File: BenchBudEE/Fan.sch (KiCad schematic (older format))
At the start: 9 parts

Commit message: Revisiting the current/fan module.
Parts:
- removed R? (x3): R, ~, symbol R
- removed RV?: POT, ~, symbol POT
- added D?: DIODE, ~, symbol DIODE
- added Q? (x2): MOSFET_N, ~, symbol MOSFET_N
- added TH?: THERMISTOR, ~, symbol THERMISTOR
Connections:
- net labels added: +12C, FAN_MODE, FAN_PWM
- net labels removed: FAN_EN_N
- wire segments 31 -> 32
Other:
- note added: "+12C non-filtered / non-current-limited"
- note added: "Filtered Rail (12V)"
- note added: "Load/Field"
- note added: "Mosfet is used to select\nVoltage or Current mode here"
- note added: "This PTC will limit max current\nthrough load."
- moved on the sheet: R?
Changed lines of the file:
@@
 $Descr A4 11693 8268
 encoding utf-8
-Sheet 9 9
+Sheet 7 9
 Title ""
-Date "10 feb 2014"
+Date "12 feb 2014"
 Rev ""
 Comp ""
@@
 Comment4 ""
 $EndDescr
-Text HLabel 10650 3700 0    60   Output ~ 0
+Text HLabel 10500 1450 2    60   Output ~ 0
 FAN_OUT+
-Text HLabel 10650 4050 0    60   Output ~ 0
+Text HLabel 10500 1750 2    60   Output ~ 0
 FAN_OUT-
-Text HLabel 10650 4500 0    60   Input ~ 0
+Text HLabel 10500 6000 2    60   Input ~ 0
 TACH_IN
-Text HLabel 1400 5600 0    60   Output ~ 0
+Text HLabel 1400 6000 0    60   Output ~ 0
 TACH_MEAS
 Text HLabel 1400 3950 0    60   Input ~ 0
-FAN_EN_N
+FAN_PWM
 $Comp
 L LM324 U?
@@
 	1    0    0    -1
 $EndComp
-$Comp
-L +12V #PWR?
-U 1 1 52F362D2
-P 7800 1700
-F 0 "#PWR?" H 7800 1650 20  0001 C CNN
-F 1 "+12V" H 7800 1800 30  0000 C CNN
-F 2 "" H 7800 1700 60  0000 C CNN
-F 3 "" H 7800 1700 60  0000 C CNN
-	1    7800 1700
-	1    0    0    -1
-$EndComp
 Wire Wire Line
 	6850 2700 7500 2700
 Wire Wire Line
-	7800 2900 7800 3700
-Wire Wire Line
-	7800 3700 10650 3700
-Wire Wire Line
-	5500 4050 10650 4050
-Wire Wire Line
-	7800 4050 7800 4300
+	7800 2900 7800 4400
 $Comp
 L R R?
 U 1 1 52F362F4
-P 7800 4550
-F 0 "R?" V 7880 4550 40  0000 C CNN
-F 1 "R" V 7807 4551 40  0000 C CNN
-F 2 "~" V 7730 4550 30  0000 C CNN
-F 3 "~" H 7800 4550 30  0000 C CNN
-	1    7800 4550
+P 7800 4650
+F 0 "R?" V 7880 4650 40  0000 C CNN
+F 1 "R" V 7807 4651 40  0000 C CNN
+F 2 "~" V 7730 4650 30  0000 C CNN
+F 3 "~" H 7800 4650 30  0000 C CNN
+	1    7800 4650
 	1    0    0    -1
 $EndComp
@@
 $EndComp
 Wire Wire Line
-	7800 5300 7800 4800
+	7800 5300 7800 4900
 Wire Wire Line
 	5500 4050 5500 2800
@@
 	5500 2800 5850 2800
 Connection ~ 7800 4050
-Wire Wire Line
-	7800 2500 7800 1700
 $Comp
 L +12V #PWR?
@@
 	4400 2600 5850 2600
 $Comp
-L R R?
-U 1 1 52F3640C
-P 4700 2200
-F 0 "R?" V 4780 2200 40  0000 C CNN
-F 1 "R" V 4707 2201 40  0000 C CNN
-F 2 "~" V 4630 2200 30  0000 C CNN
-F 3 "~" H 4700 2200 30  0000 C CNN
-	1    4700 2200
-	1    0    0    -1
-$EndComp
-$Comp
-L +12V #PWR?
-U 1 1 52F36412
-P 4700 1750
-F 0 "#PWR?" H 4700 1700 20  0001 C CNN
-F 1 "+12V" H 4700 1850 30  0000 C CNN
-F 2 "" H 4700 1750 60  0000 C CNN
-F 3 "" H 4700 1750 60  0000 C CNN
-	1    4700 1750
-	1    0    0    -1
-$EndComp
-Wire Wire Line
-	4700 1750 4700 1950
-Wire Wire Line
-	4700 2450 4700 2900
-$Comp
-L POT RV?
-U 1 1 52F36438
-P 4700 3150
-F 0 "RV?" H 4700 3050 50  0000 C CNN
-F 1 "POT" H 4700 3150 50  0000 C CNN
-F 2 "~" H 4700 3150 60  0000 C CNN
-F 3 "~" H 4700 3150 60  0000 C CNN
-	1    4700 3150
-	0    -1   -1   0
-$EndComp
-Connection ~ 4700 2600
-$Comp
 L AGND #PWR?
 U 1 1 52F36460
-P 4700 3700
-F 0 "#PWR?" H 4700 3700 40  0001 C CNN
-F 1 "AGND" H 4700 3630 50  0000 C CNN
-F 2 "" H 4700 3700 60  0000 C CNN
-F 3 "" H 4700 3700 60  0000 C CNN
-	1    4700 3700
-	1    0    0    -1
-$EndComp
-Wire Wire Line
-	4700 3700 4700 3400
+P 5150 3700
+F 0 "#PWR?" H 5150 3700 40  0001 C CNN
+F 1 "AGND" H 5150 3630 50  0000 C CNN
+F 2 "" H 5150 3700 60  0000 C CNN
+F 3 "" H 5150 3700 60  0000 C CNN
+	1    5150 3700
+	1    0    0    -1
+$EndComp
 $Comp
 L MCP4922-E/P U?
@@
 	1    0    0    -1
 $EndComp
-Wire Wire Line
-	10650 4500 9500 4500
-Wire Wire Line
-	9500 4500 9500 5850
-Wire Wire Line
-	9500 5850 2050 5850
 Text HLabel 1400 4200 0    60   Output ~ 0
 CURR_MEAS
 Wire Wire Line
-	2050 5850 2050 5600
-Wire Wire Line
 	1400 4200 7800 4200
 Connection ~ 7800 4200
-Wire Wire Line
-	2050 5600 1400 5600
 Connection ~ 5150 2600
 Wire Wire Line
-	1400 3950 5150 3950
-$Comp
-L R R?
-U 1 1 52F36597
-P 5150 3150
-F 0 "R?" V 5230 3150 40  0000 C CNN
-F 1 "R" V 5157 3151 40  0000 C CNN
-F 2 "~" V 5080 3150 30  0000 C CNN
-F 3 "~" H 5150 3150 30  0000 C CNN
-	1    5150 3150
-	1    0    0    -1
-$EndComp
-Wire Wire Line
-	5150 2900 5150 2600
-Wire Wire Line
-	5150 3950 5150 3400
+	5150 2600 5150 2950
 $Comp
 L R R?
@@
 Wire Wire Line
 	1400 2750 2400 2750
-$Comp
-L R R?
-U 1 1 52F36679
-P 2200 3400
-F 0 "R?" V 2280 3400 40  0000 C CNN
-F 1 "R" V 2207 3401 40  0000 C CNN
-F 2 "~" V 2130 3400 30  0000 C CNN
-F 3 "~" H 2200 3400 30  0000 C CNN
-	1    2200 3400
-	1    0    0    -1
-$EndComp
-Wire Wire Line
-	2400 2950 2200 2950
-Wire Wire Line
-	2200 2950 2200 3150
-Wire Wire Line
-	2200 3650 2200 3950
-Connection ~ 2200 3950
 Text Notes 2850 1950 0    60   ~ 0
 DAC
+$Comp
+L MOSFET_N Q?
+U 1 1 52FADC41
+P 7200 4650
+F 0 "Q?" H 7210 4820 60  0000 R CNN
+F 1 "MOSFET_N" H 7210 4500 60  0000 R CNN
+F 2 "~" H 7200 4650 60  0000 C CNN
+F 3 "~" H 7200 4650 60  0000 C CNN
+	1    7200 4650
+	1    0    0    -1
+$EndComp
+$Comp
+L THERMISTOR TH?
+U 1 1 52FADC53
+P 7800 1100
+F 0 "TH?" V 7900 1150 50  0000 C CNN
+F 1 "THERMISTOR" V 7700 1100 50  0000 C CNN
+F 2 "~" H 7800 1100 60  0000 C CNN
+F 3 "~" H 7800 1100 60  0000 C CNN
+	1    7800 1100
+	1    0    0    -1
+$EndComp
+Wire Wire Line
+	7800 850  7800 750
+Wire Wire Line
+	7800 1350 7800 1450
+Wire Wire Line
+	7350 1450 10500 1450
+Wire Wire Line
+	10500 1750 7800 1750
+Wire Wire Line
+	7800 1750 7800 2500
+$Comp
+L DIODE D?
+U 1 1 52FADCC6
+P 7350 1650
+F 0 "D?" H 7350 1750 40  0000 C CNN
+F 1 "DIODE" H 7350 1550 40  0000 C CNN
+F 2 "~" H 7350 1650 60  0000 C CNN
+F 3 "~" H 7350 1650 60  0000 C CNN
+	1    7350 1650
+	0    -1   -1   0
+$EndComp
+Wire Wire Line
+	7350 1850 7800 1850
+Connection ~ 7800 1850
+Connection ~ 7800 1450
+Wire Wire Line
+	5500 4050 7800 4050
+Wire Wire Line
+	7800 4050 7800 4100
+Wire Wire Line
+	7300 4450 7300 4350
+Wire Wire Line
+	7300 4350 7800 4350
+Connection ~ 7800 4350
+Wire Wire Line
+	7300 4850 7300 5050
+Wire Wire Line
+	7300 5050 7800 5050
+Connection ~ 7800 5050
+Wire Wire Line
+	1400 6000 10500 6000
+$Comp
+L MOSFET_N Q?
+U 1 1 52FAE0E1
+P 5050 3150
+F 0 "Q?" H 5060 3320 60  0000 R CNN
+F 1 "MOSFET_N" H 5060 3000 60  0000 R CNN
+F 2 "~" H 5050 3150 60  0000 C CNN
+F 3 "~" H 5050 3150 60  0000 C CNN
+	1    5050 3150
+	1    0    0    -1
+$EndComp
+Wire Wire Line
+	5150 3700 5150 3350
+Wire Wire Line
+	1400 3950 4050 3950
+Wire Wire Line
+	4050 3950 4050 3150
+Wire Wire Line
+	4050 3150 4850 3150
+Wire Wire Line
+	7000 4650 1400 4650
+Text HLabel 1400 4650 0    60   Input ~ 0
+FAN_MODE
+Text Notes 5850 1600 0    60   ~ 0
+Filtered Rail (12V)
+$Comp
+L +12C #PWR?
+U 1 1 52FAE969
+P 7800 750
+F 0 "#PWR?" H 7800 720 30  0001 C CNN
+F 1 "+12C" H 7800 860 40  0000 C CNN
+F 2 "" H 7800 750 60  0000 C CNN
+F 3 "" H 7800 750 60  0000 C CNN
+	1    7800 750
+	1    0    0    -1
+$EndComp
+Text Notes 8000 1000 0    60   ~ 0
+This PTC will limit max current\nthrough load.
+Text Notes 10150 1650 0    60   ~ 0
+Load/Field
+Text Notes 8050 4650 0    60   ~ 0
+Mosfet is used to select\nVoltage or Current mode here
+Text Notes 7950 650  0    60   ~ 0
++12C non-filtered / non-current-limited
 $EndSCHEMATC

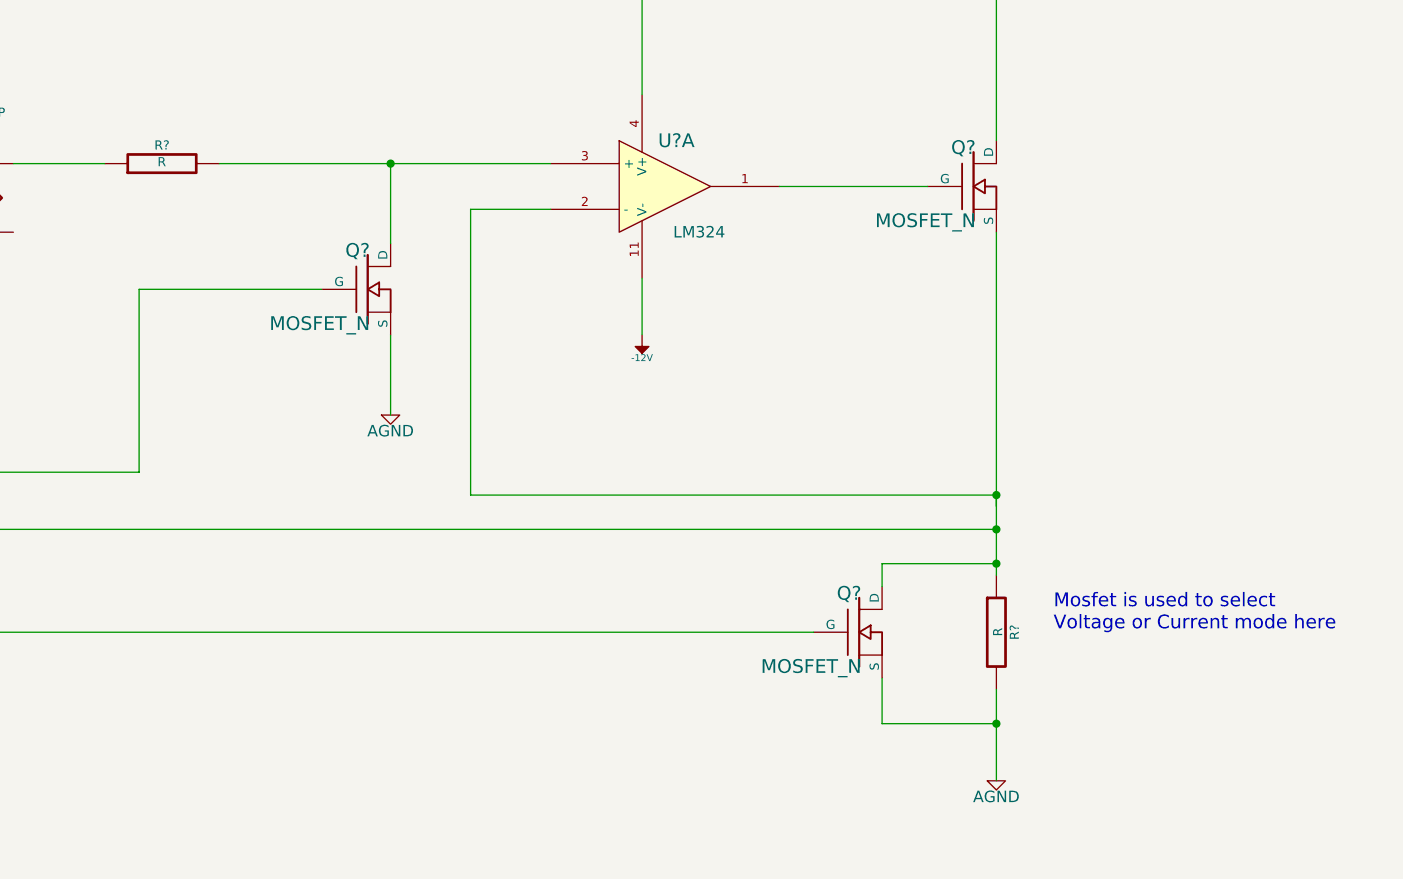
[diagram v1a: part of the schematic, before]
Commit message: Documented the fan driver mosfets.
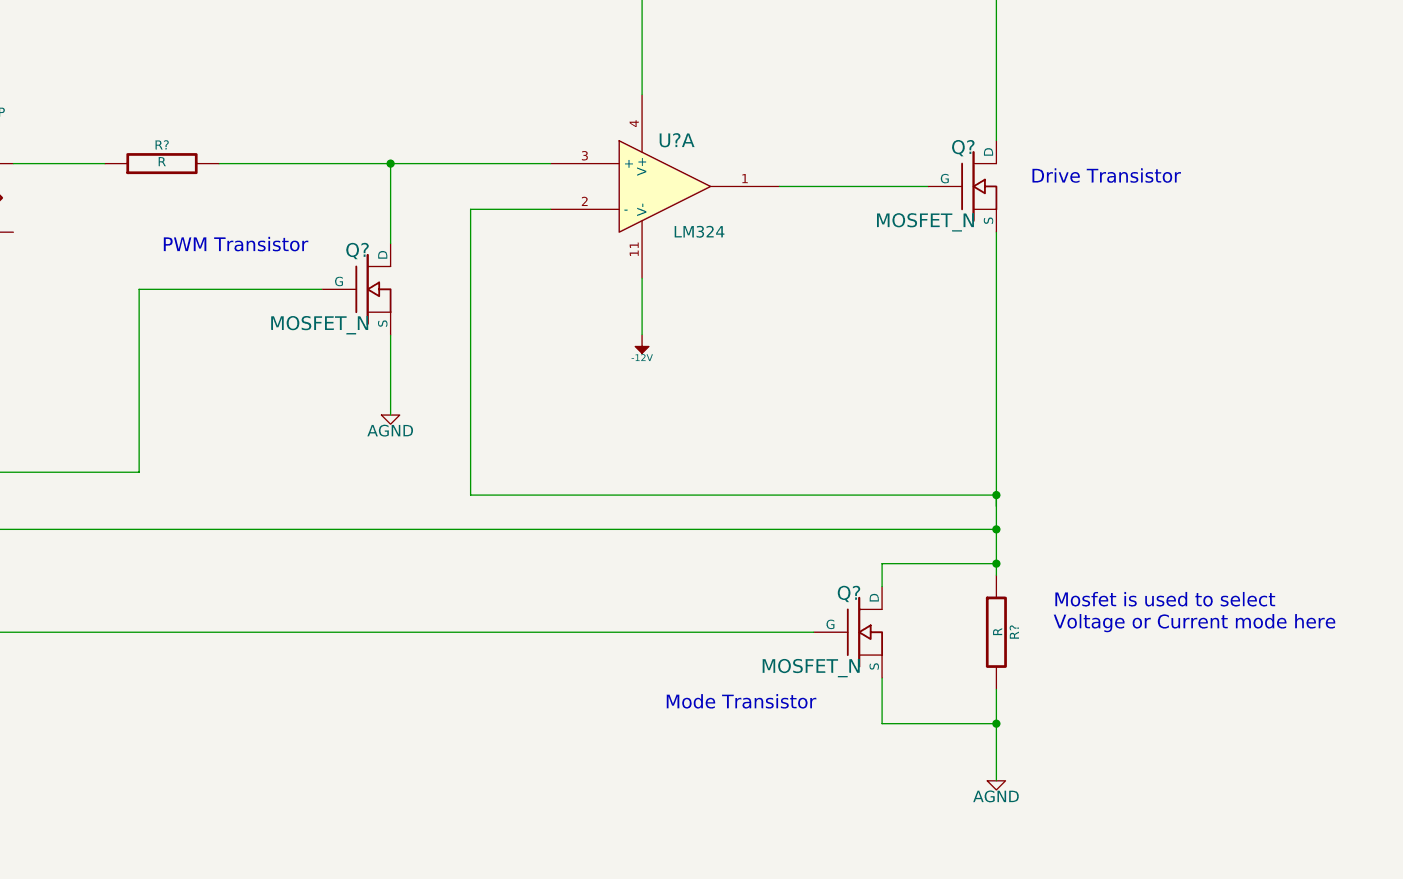
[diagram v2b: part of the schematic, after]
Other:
- note added: "Drive Transistor"
- note added: "Mode Transistor"
- note added: "PWM Transistor"
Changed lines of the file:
@@
 Sheet 7 9
 Title ""
-Date "12 feb 2014"
+Date "14 feb 2014"
 Rev ""
 Comp ""
@@
 Text Notes 7950 650  0    60   ~ 0
 +12C non-filtered / non-current-limited
+Text Notes 7950 2700 0    60   ~ 0
+Drive Transistor
+Text Notes 4150 3000 0    60   ~ 0
+PWM Transistor
+Text Notes 6350 5000 0    60   ~ 0
+Mode Transistor
 $EndSCHEMATC

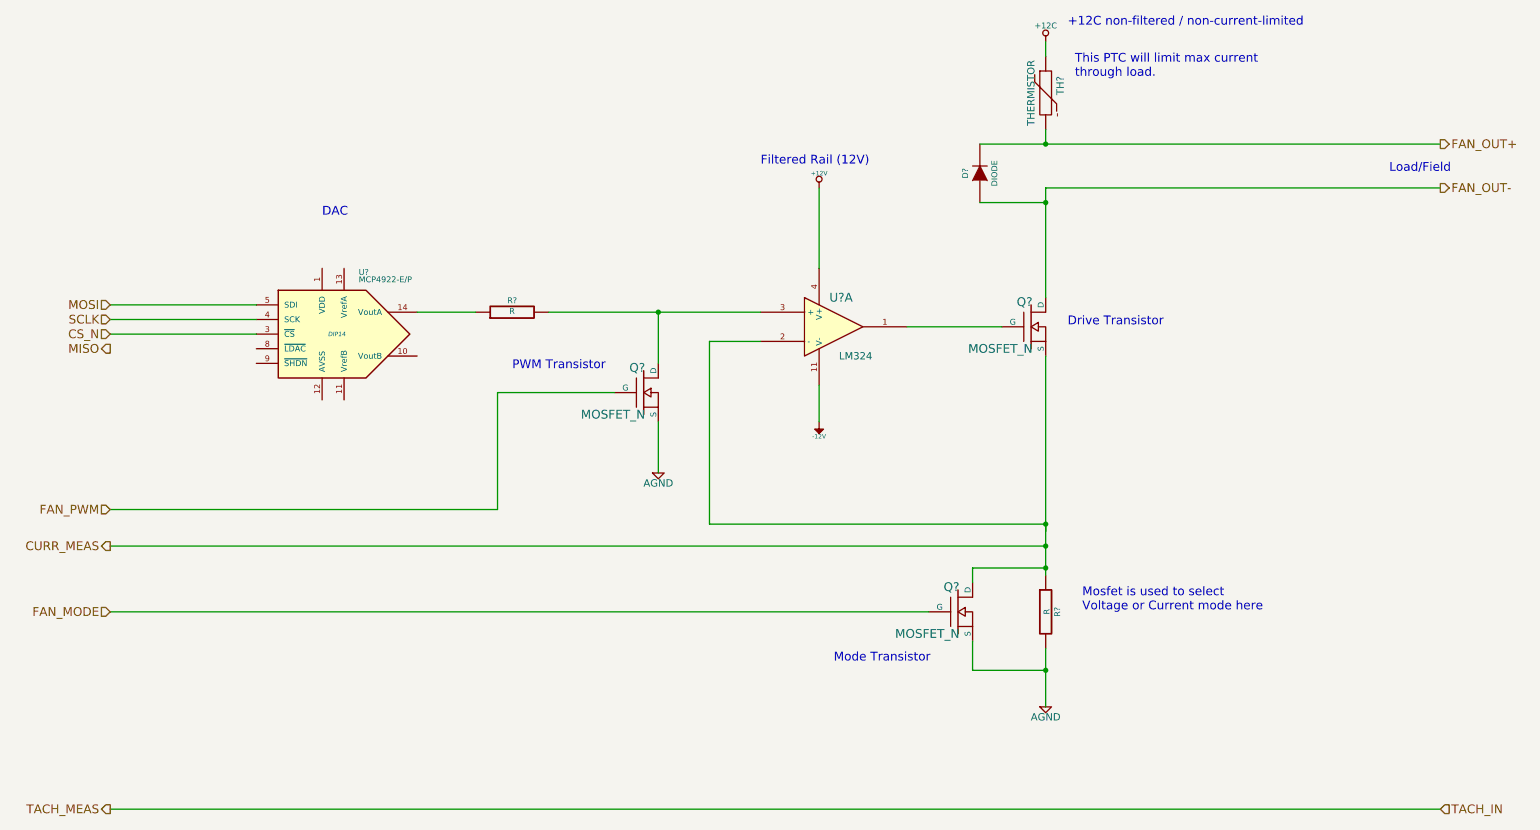
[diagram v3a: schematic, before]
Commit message: Placed the relay components.
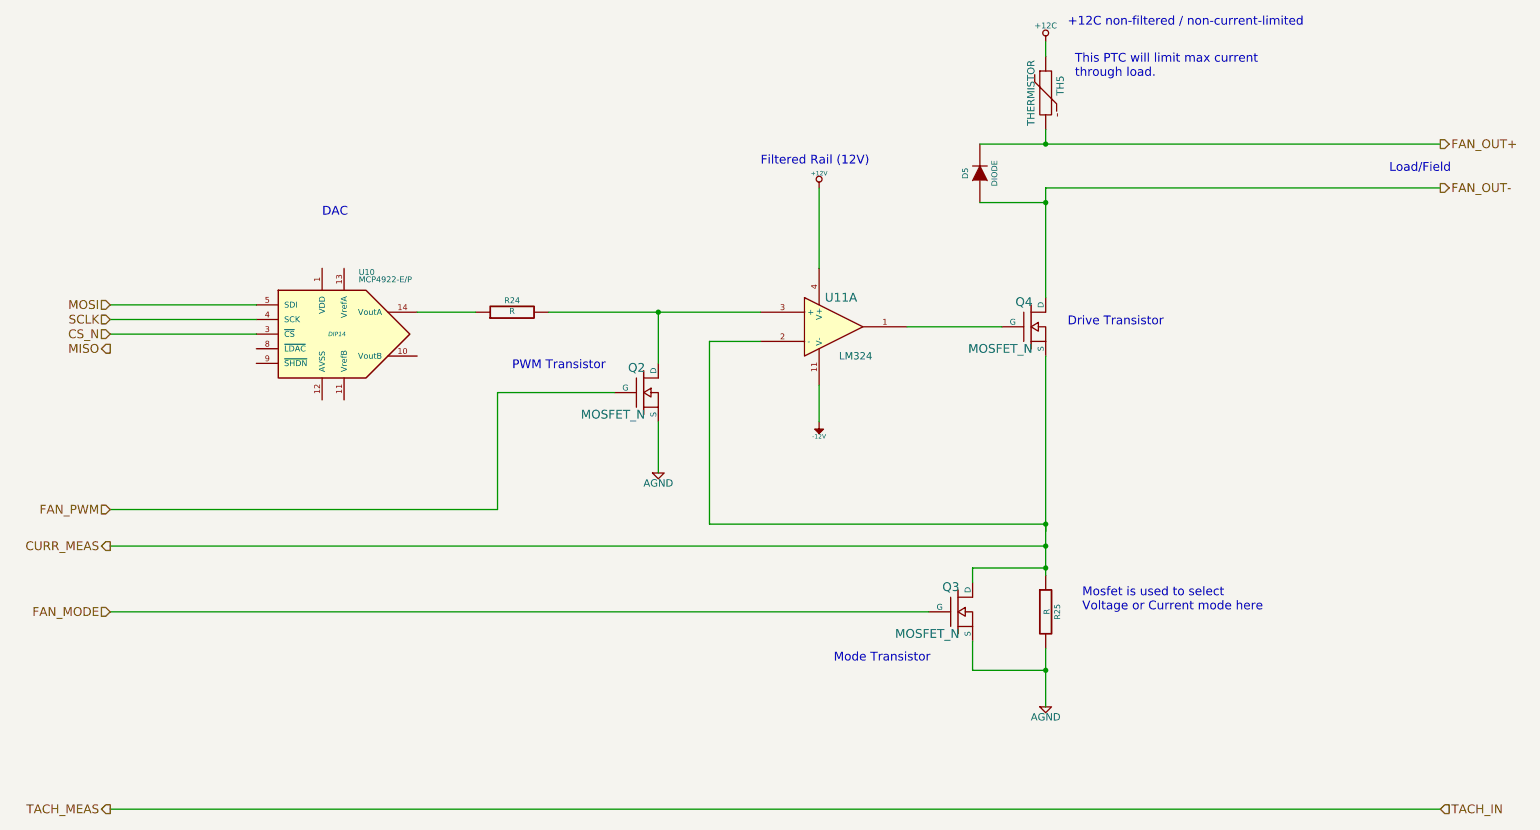
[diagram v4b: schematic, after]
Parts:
- gave numbers to parts that had none: 9
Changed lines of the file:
@@
 Sheet 7 9
 Title ""
-Date "19 feb 2014"
+Date "20 feb 2014"
 Rev ""
 Comp ""
@@
 FAN_PWM
 $Comp
-L LM324 U?
+L LM324 U11
 U 1 1 52F36291
 P 6350 2700
-F 0 "U?" H 6400 2900 60  0000 C CNN
+F 0 "U11" H 6400 2900 60  0000 C CNN
 F 1 "LM324" H 6500 2500 50  0000 C CNN
 F 2 "" H 6350 2700 60  0000 C CNN
@@
 $EndComp
 $Comp
-L MOSFET_N Q?
+L MOSFET_N Q4
 U 1 1 52F362B9
 P 7700 2700
-F 0 "Q?" H 7710 2870 60  0000 R CNN
+F 0 "Q4" H 7710 2870 60  0000 R CNN
 F 1 "MOSFET_N" H 7710 2550 60  0000 R CNN
 F 2 "~" H 7700 2700 60  0000 C CNN
@@
 	7800 2900 7800 4400
 $Comp
-L R R?
+L R R25
 U 1 1 52F362F4
 P 7800 4650
-F 0 "R?" V 7880 4650 40  0000 C CNN
+F 0 "R25" V 7880 4650 40  0000 C CNN
 F 1 "R" V 7807 4651 40  0000 C CNN
 F 2 "~" V 7730 4650 30  0000 C CNN
@@
 $EndComp
 $Comp
-L AGND #PWR?
+L AGND #PWR48
 U 1 1 52F3630D
 P 7800 5300
-F 0 "#PWR?" H 7800 5300 40  0001 C CNN
+F 0 "#PWR48" H 7800 5300 40  0001 C CNN
 F 1 "AGND" H 7800 5230 50  0000 C CNN
 F 2 "" H 7800 5300 60  0000 C CNN
@@
 Connection ~ 7800 4050
 $Comp
-L +12V #PWR?
+L +12V #PWR45
 U 1 1 52F36343
 P 6250 1750
-F 0 "#PWR?" H 6250 1700 20  0001 C CNN
+F 0 "#PWR45" H 6250 1700 20  0001 C CNN
 F 1 "+12V" H 6250 1850 30  0000 C CNN
 F 2 "" H 6250 1750 60  0000 C CNN
@@
 	6250 1750 6250 2300
 $Comp
-L -12V #PWR?
+L -12V #PWR46
 U 1 1 52F36356
 P 6250 3350
-F 0 "#PWR?" H 6250 3480 20  0001 C CNN
+F 0 "#PWR46" H 6250 3480 20  0001 C CNN
 F 1 "-12V" H 6250 3450 30  0000 C CNN
 F 2 "" H 6250 3350 60  0000 C CNN
@@
 	4400 2600 5850 2600
 $Comp
-L AGND #PWR?
+L AGND #PWR44
 U 1 1 52F36460
 P 5150 3700
-F 0 "#PWR?" H 5150 3700 40  0001 C CNN
+F 0 "#PWR44" H 5150 3700 40  0001 C CNN
 F 1 "AGND" H 5150 3630 50  0000 C CNN
 F 2 "" H 5150 3700 60  0000 C CNN
@@
 $EndComp
 $Comp
-L MCP4922-E/P U?
+L MCP4922-E/P U10
 U 1 1 52F36479
 P 2950 2750
-F 0 "U?" H 3100 3150 40  0000 L BNN
+F 0 "U10" H 3100 3150 40  0000 L BNN
 F 1 "MCP4922-E/P" H 3100 3100 40  0000 L BNN
 F 2 "DIP14" H 2950 2750 30  0000 C CIN
@@
 	5150 2600 5150 2950
 $Comp
-L R R?
+L R R24
 U 1 1 52F365D4
 P 4150 2600
-F 0 "R?" V 4230 2600 40  0000 C CNN
+F 0 "R24" V 4230 2600 40  0000 C CNN
 F 1 "R" V 4157 2601 40  0000 C CNN
 F 2 "~" V 4080 2600 30  0000 C CNN
@@
 DAC
 $Comp
-L MOSFET_N Q?
+L MOSFET_N Q3
 U 1 1 52FADC41
 P 7200 4650
-F 0 "Q?" H 7210 4820 60  0000 R CNN
+F 0 "Q3" H 7210 4820 60  0000 R CNN
 F 1 "MOSFET_N" H 7210 4500 60  0000 R CNN
 F 2 "~" H 7200 4650 60  0000 C CNN
@@
 $EndComp
 $Comp
-L THERMISTOR TH?
+L THERMISTOR TH5
 U 1 1 52FADC53
 P 7800 1100
-F 0 "TH?" V 7900 1150 50  0000 C CNN
+F 0 "TH5" V 7900 1150 50  0000 C CNN
 F 1 "THERMISTOR" V 7700 1100 50  0000 C CNN
 F 2 "~" H 7800 1100 60  0000 C CNN
@@
 	7800 1750 7800 2500
 $Comp
-L DIODE D?
+L DIODE D5
 U 1 1 52FADCC6
 P 7350 1650
-F 0 "D?" H 7350 1750 40  0000 C CNN
+F 0 "D5" H 7350 1750 40  0000 C CNN
 F 1 "DIODE" H 7350 1550 40  0000 C CNN
 F 2 "~" H 7350 1650 60  0000 C CNN
@@
 	1400 6000 10500 6000
 $Comp
-L MOSFET_N Q?
+L MOSFET_N Q2
 U 1 1 52FAE0E1
 P 5050 3150
-F 0 "Q?" H 5060 3320 60  0000 R CNN
+F 0 "Q2" H 5060 3320 60  0000 R CNN
 F 1 "MOSFET_N" H 5060 3000 60  0000 R CNN
 F 2 "~" H 5050 3150 60  0000 C CNN
@@
 Filtered Rail (12V)
 $Comp
-L +12C #PWR?
+L +12C #PWR47
 U 1 1 52FAE969
 P 7800 750
-F 0 "#PWR?" H 7800 720 30  0001 C CNN
+F 0 "#PWR47" H 7800 720 30  0001 C CNN
 F 1 "+12C" H 7800 860 40  0000 C CNN
 F 2 "" H 7800 750 60  0000 C CNN
